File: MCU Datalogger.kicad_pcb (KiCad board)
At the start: 2 copper layers, 51.6 x 36 mm, 30 parts, among them J1 Conn_01x04_Pin, J2 Conn_01x09_Pin, J3 Conn_01x04_Pin, J4 Conn_02x03_Odd_Even, U1 24LC1025, U2 DS1337S_, U3 24LC1025, U4 ATMEGA328P-AU, Y1 32.768 KHz, Y2 16 MHz

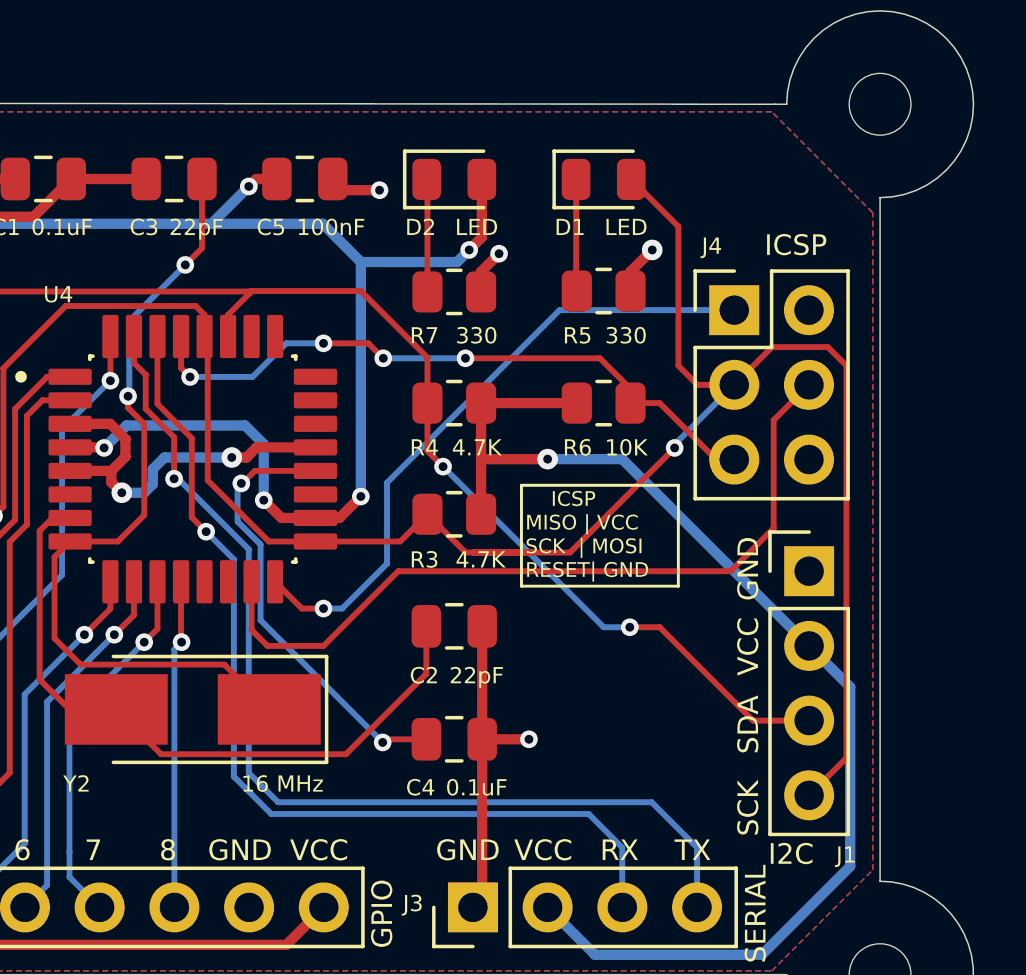
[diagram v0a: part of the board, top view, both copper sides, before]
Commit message: Fixed  2 layer PCB.
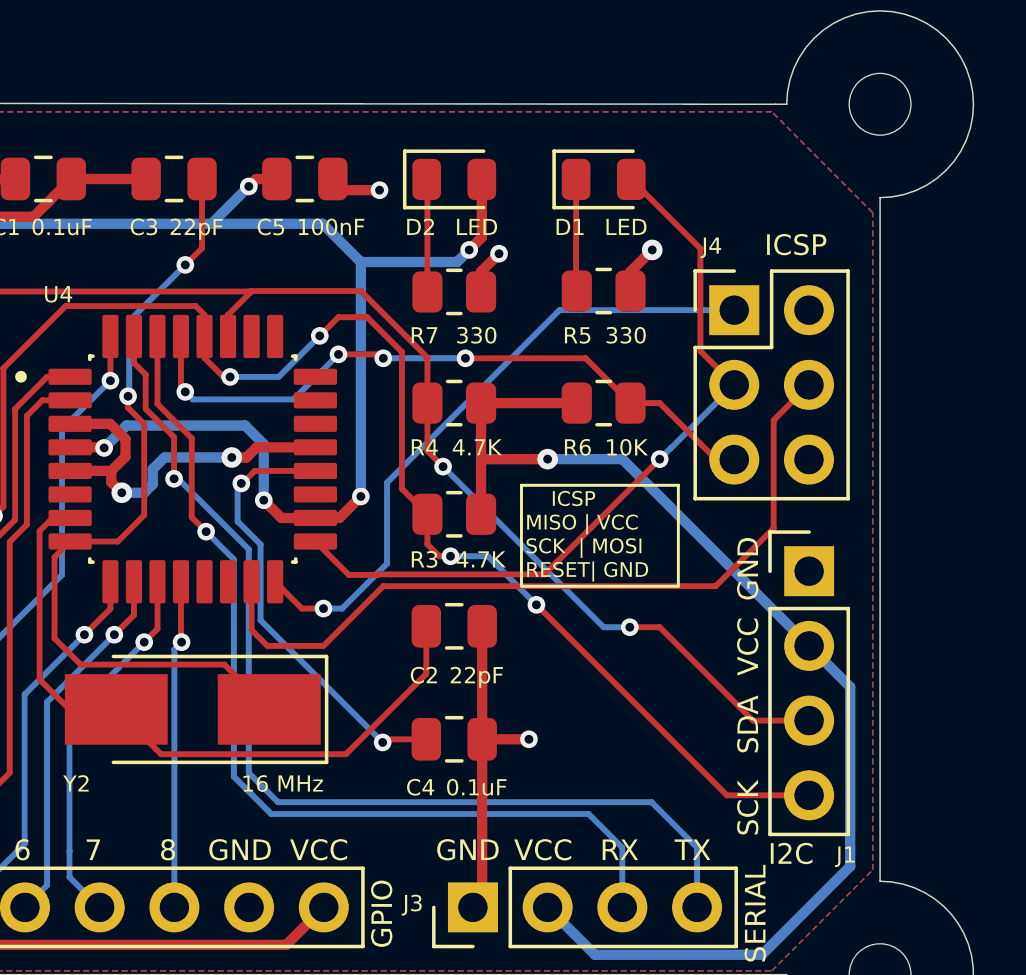
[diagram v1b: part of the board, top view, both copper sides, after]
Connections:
- J1 pad 4: /SCK -> /SCL
- R3 pad 2: /SCK -> /SCL
- U1 pad 6: /SCK -> /SCL
- U2 pad 6: /SCK -> /SCL
- U3 pad 6: /SCK -> /SCL
- U4 pad 28: /SCK -> /SCL
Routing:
- net /SCK: track 103.1 -> 25.8 mm, vias 3 -> 1
- net /SCL: track 0.00 -> 75.7 mm, vias 0 -> 6
- net GND: track 68.2 -> 67.6 mm

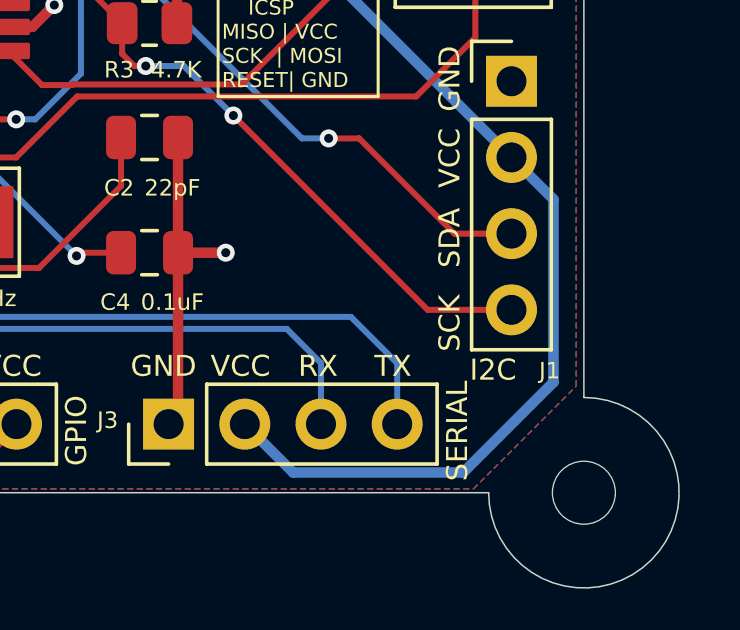
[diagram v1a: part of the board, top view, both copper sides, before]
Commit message: Changed SCK label to SCL for I2C.
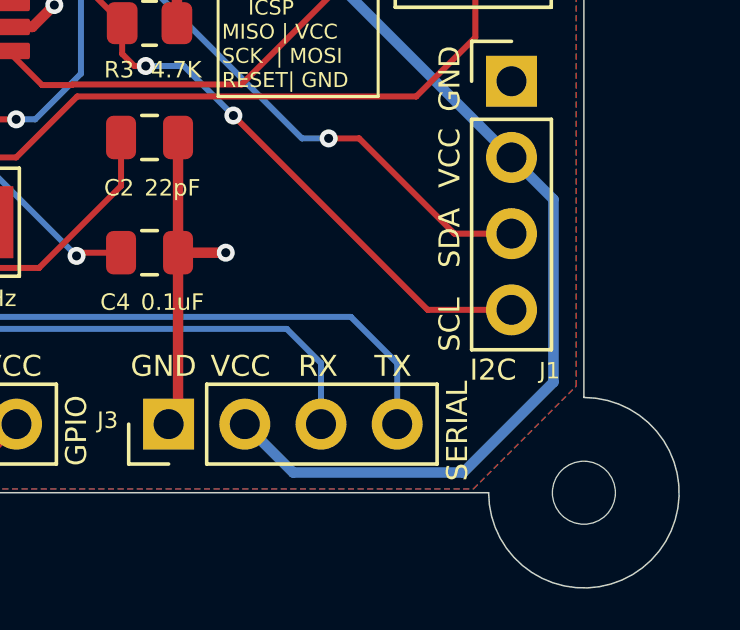
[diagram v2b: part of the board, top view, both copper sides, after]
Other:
- board text added: "SCL"
- board text removed: "SCK"
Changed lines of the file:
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@@
 		)
 	)
-	(gr_text "SCK"
+	(gr_text "SCL"
 		(at 196.469 111.252 90)
 		(layer "F.SilkS")

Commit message: Finished 2layer PCB project.
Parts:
- moved BT1 85.6 mm to (72.7, 89.6)
- moved C1 85.6 mm to (86.7, 83.8)
- moved C2 85.6 mm to (100.6, 99.1)
- moved C4 85.6 mm to (100.6, 102.9)
- moved D2 85.6 mm to (100.6, 83.9)
- moved H2 85.6 mm to (69.9, 110.9)
- moved J1 85.6 mm to (112.7, 97.2)
- moved J2 85.6 mm to (75.9, 108.6)
- moved R3 85.6 mm to (100.6, 95.2)
- moved R4 85.6 mm to (100.6, 91.5)
- moved R7 85.6 mm to (100.6, 87.7)
- moved U2 85.6 mm to (79.4, 100.4)
- moved Y1 85.6 mm to (72.7, 101.0)
- moved C3 85.6 mm to (91.1, 83.8)
- moved C5 85.6 mm to (95.6, 83.8)
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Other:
- board text added: "0.0000 mm / 0.0000 mm"
- board text added: "0.3000 mm"
- board text added: "1.6000 mm"
- board text added: "51.5980 mm x 35.9770 mm"
- board text added: "BOARD CHARACTERISTICS"
- board text added: "Board Thickness:"
- board text added: "Board overall dimensions:"
- board text added: "Castellated pads:"
- board text added: "Copper Finish:"
- board text added: "Copper Layer Count:"
- board text added: "Edge card connectors:"
- board text added: "Impedance Control:"
- board text added: "Min hole diameter:"
- board text added: "Min track/spacing:"
- board text added: "No"
- board text added: "None"
- board text added: "Plated Board Edge:"

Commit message: Added B silkscreen text.
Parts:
- added REF**: KiCad-Logo2_5mm_SilkScreen, Symbol:KiCad-Logo2_5mm_SilkScreen, B.Cu at (92.6, 88.0)
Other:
- board text added: "Data logger with ATMega328P."
